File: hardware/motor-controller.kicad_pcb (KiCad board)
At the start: 2 copper layers, 45 parts, among them P102 SWD, P103 EDISON-BULB-E10, P104 FTDI-PLUG, U201 IRLML2803TRPBF, U202 IRLML2803TRPBF, U203 7408, U204 MC33926, U205 MC33926, U206 74AHC541D

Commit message: add footprints for motor connectors
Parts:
- added P201: P06-MOTOR, kicadlib:JST-S6B-PH-K, F.Cu at (144.5, 88.9)
- added P202: P06-MOTOR, kicadlib:JST-S6B-PH-K, F.Cu at (166.8, 85.9)
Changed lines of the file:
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@@
 (kicad_pcb (version 4) (host pcbnew "(after 2015-may-25 BZR unknown)-product")
   (general
-    (links 132)
-    (no_connects 132)
+    (links 144)
+    (no_connects 144)
     (area 0 0 0 0)
     (thickness 1.6)
@@
     (tracks 0)
     (zones 0)
-    (modules 45)
+    (modules 47)
     (nets 69)
   )
@@
       (net 1 +3.3V))
   )
+  (module kicadlib:JST-S6B-PH-K (layer F.Cu)
+    (at 144.5 88.9)
+    (fp_text reference P201 (at -4.8 1.2) (layer F.SilkS)
+      (effects (font (size 0.6 0.6) (thickness 0.1)))
+    )
+    (fp_text value P06-MOTOR (at 0 -2.8) (layer F.Fab)
+      (effects (font (size 0.6 0.6) (thickness 0.1)))
+    )
+    (fp_line (start -7.2 -11.4) (end -7.2 1.8) (layer F.CrtYd) (width 0.15))
+    (fp_line (start -7.2 1.8) (end 7.2 1.8) (layer F.CrtYd) (width 0.15))
+    (fp_line (start 7.2 1.8) (end 7.2 -11.4) (layer F.CrtYd) (width 0.15))
+    (fp_line (start 7.2 -11.4) (end -7.2 -11.4) (layer F.CrtYd) (width 0.15))
+    (fp_line (start 6.95 1.6) (end 6.2 1.6) (layer F.SilkS) (width 0.15))
+    (fp_line (start 6.2 1.6) (end 6.2 0) (layer F.SilkS) (width 0.15))
+    (fp_line (start -6.95 1.6) (end -6.2 1.6) (layer F.SilkS) (width 0.15))
+    (fp_line (start -6.2 1.6) (end -6.2 0) (layer F.SilkS) (width 0.15))
+    (fp_line (start -6.2 0) (end 6.2 0) (layer F.SilkS) (width 0.15))
+    (fp_line (start -6.95 -6) (end 6.95 -6) (layer F.SilkS) (width 0.15))
+    (fp_line (start 6.95 -6) (end 6.95 1.6) (layer F.SilkS) (width 0.15))
+    (fp_line (start -6.95 -6) (end -6.95 1.6) (layer F.SilkS) (width 0.15))
+    (pad 1 thru_hole circle (at 5 0) (size 1.3 1.3) (drill 0.7) (layers *.Cu *.Mask F.SilkS)
+      (net 46 "Net-(P201-Pad1)"))
+    (pad 2 thru_hole circle (at 3 0) (size 1.3 1.3) (drill 0.7) (layers *.Cu *.Mask F.SilkS)
+      (net 49 "Net-(P201-Pad2)"))
+    (pad 3 thru_hole circle (at 1 0) (size 1.3 1.3) (drill 0.7) (layers *.Cu *.Mask F.SilkS)
+      (net 11 +5V))
+    (pad 4 thru_hole circle (at -1 0) (size 1.3 1.3) (drill 0.7) (layers *.Cu *.Mask F.SilkS)
+      (net 2 GNDPWR))
+    (pad 5 thru_hole circle (at -3 0) (size 1.3 1.3) (drill 0.7) (layers *.Cu *.Mask F.SilkS)
+      (net 57 "Net-(P201-Pad5)"))
+    (pad 6 thru_hole circle (at -5 0) (size 1.3 1.3) (drill 0.7) (layers *.Cu *.Mask F.SilkS)
+      (net 58 "Net-(P201-Pad6)"))
+  )
+  (module kicadlib:JST-S6B-PH-K (layer F.Cu)
+    (at 166.8 85.9)
+    (fp_text reference P202 (at -4.8 1.2) (layer F.SilkS)
+      (effects (font (size 0.6 0.6) (thickness 0.1)))
+    )
+    (fp_text value P06-MOTOR (at 0 -2.8) (layer F.Fab)
+      (effects (font (size 0.6 0.6) (thickness 0.1)))
+    )
+    (fp_line (start -7.2 -11.4) (end -7.2 1.8) (layer F.CrtYd) (width 0.15))
+    (fp_line (start -7.2 1.8) (end 7.2 1.8) (layer F.CrtYd) (width 0.15))
+    (fp_line (start 7.2 1.8) (end 7.2 -11.4) (layer F.CrtYd) (width 0.15))
+    (fp_line (start 7.2 -11.4) (end -7.2 -11.4) (layer F.CrtYd) (width 0.15))
+    (fp_line (start 6.95 1.6) (end 6.2 1.6) (layer F.SilkS) (width 0.15))
+    (fp_line (start 6.2 1.6) (end 6.2 0) (layer F.SilkS) (width 0.15))
+    (fp_line (start -6.95 1.6) (end -6.2 1.6) (layer F.SilkS) (width 0.15))
+    (fp_line (start -6.2 1.6) (end -6.2 0) (layer F.SilkS) (width 0.15))
+    (fp_line (start -6.2 0) (end 6.2 0) (layer F.SilkS) (width 0.15))
+    (fp_line (start -6.95 -6) (end 6.95 -6) (layer F.SilkS) (width 0.15))
+    (fp_line (start 6.95 -6) (end 6.95 1.6) (layer F.SilkS) (width 0.15))
+    (fp_line (start -6.95 -6) (end -6.95 1.6) (layer F.SilkS) (width 0.15))
+    (pad 1 thru_hole circle (at 5 0) (size 1.3 1.3) (drill 0.7) (layers *.Cu *.Mask F.SilkS)
+      (net 53 "Net-(P202-Pad1)"))
+    (pad 2 thru_hole circle (at 3 0) (size 1.3 1.3) (drill 0.7) (layers *.Cu *.Mask F.SilkS)
+      (net 56 "Net-(P202-Pad2)"))
+    (pad 3 thru_hole circle (at 1 0) (size 1.3 1.3) (drill 0.7) (layers *.Cu *.Mask F.SilkS)
+      (net 11 +5V))
+    (pad 4 thru_hole circle (at -1 0) (size 1.3 1.3) (drill 0.7) (layers *.Cu *.Mask F.SilkS)
+      (net 2 GNDPWR))
+    (pad 5 thru_hole circle (at -3 0) (size 1.3 1.3) (drill 0.7) (layers *.Cu *.Mask F.SilkS)
+      (net 59 "Net-(P202-Pad5)"))
+    (pad 6 thru_hole circle (at -5 0) (size 1.3 1.3) (drill 0.7) (layers *.Cu *.Mask F.SilkS)
+      (net 60 "Net-(P202-Pad6)"))
+  )
 )

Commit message: add package for battery and compass
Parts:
- added P101: BATTERY, kicadlib:TECONN-2-1445098-2, F.Cu at (116.5, 91.8)
- added U101: STM32F030K6T6, kicadlib:QFP80P900X900X160-32N, F.Cu at (151.0, 117.2)
- added U102: ST-LIS3MDL, kicadlib:LGA12S50P4X4_192X192X100, F.Cu at (187.7, 85.8)
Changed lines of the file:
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@@
 (kicad_pcb (version 4) (host pcbnew "(after 2015-may-25 BZR unknown)-product")
   (general
-    (links 144)
-    (no_connects 144)
+    (links 185)
+    (no_connects 185)
     (area 0 0 0 0)
     (thickness 1.6)
@@
     (tracks 0)
     (zones 0)
-    (modules 47)
-    (nets 69)
+    (modules 50)
+    (nets 74)
   )
   (page A4)
@@
   (net 67 /drivers/MOTORLCHB)
   (net 68 /drivers/MOTORLCHA)
+  (net 69 "Net-(U101-Pad2)")
+  (net 70 "Net-(U101-Pad3)")
+  (net 71 "Net-(U101-Pad6)")
+  (net 72 /COMPASSDRDY)
+  (net 73 /COMPASSINT)
   (net_class Default "This is the default net class."
     (clearance 0.2)
@@
     (add_net +3.3V)
     (add_net +5V)
+    (add_net /COMPASSDRDY)
+    (add_net /COMPASSINT)
     (add_net /I2CSCL)
     (add_net /I2CSDA)
@@
     (add_net "Net-(R213-Pad1)")
     (add_net "Net-(R214-Pad1)")
+    (add_net "Net-(U101-Pad2)")
+    (add_net "Net-(U101-Pad3)")
+    (add_net "Net-(U101-Pad6)")
     (add_net "Net-(U203-Pad11)")
     (add_net "Net-(U203-Pad3)")
@@
       (net 60 "Net-(P202-Pad6)"))
   )
+  (module kicadlib:TECONN-2-1445098-2 (layer F.Cu)
+    (at 116.5 91.8)
+    (fp_text reference P101 (at 7.112 -1.27 90) (layer F.SilkS)
+      (effects (font (size 0.6 0.6) (thickness 0.1)))
+    )
+    (fp_text value BATTERY (at 1.397 -1.905) (layer F.Fab)
+      (effects (font (size 0.6 0.6) (thickness 0.1)))
+    )
+    (fp_line (start -3.57 -7.75) (end -3.57 0) (layer F.SilkS) (width 0.1))
+    (fp_line (start 6.57 0) (end 6.57 -7.75) (layer F.SilkS) (width 0.1))
+    (fp_line (start -4.07 -9.42) (end 7.07 -9.42) (layer F.CrtYd) (width 0.1))
+    (fp_line (start 7.07 -9.42) (end 7.07 1.325) (layer F.CrtYd) (width 0.1))
+    (fp_line (start 7.07 1.325) (end -4.07 1.325) (layer F.CrtYd) (width 0.1))
+    (fp_line (start -4.07 1.325) (end -4.07 -9.42) (layer F.CrtYd) (width 0.1))
+    (fp_line (start -3.57 -8.92) (end 6.57 -8.92) (layer Dwgs.User) (width 0.1))
+    (fp_line (start 6.57 -8.92) (end 6.57 -7.75) (layer Dwgs.User) (width 0.1))
+    (fp_line (start 6.57 0) (end -3.57 0) (layer F.SilkS) (width 0.1))
+    (fp_line (start -3.57 -7.75) (end -3.57 -8.92) (layer Dwgs.User) (width 0.1))
+    (pad 1 thru_hole circle (at 0 0) (size 1.65 1.65) (drill 1) (layers *.Cu *.Mask F.SilkS)
+      (net 4 Vcc))
+    (pad 2 thru_hole circle (at 3 0) (size 1.65 1.65) (drill 1) (layers *.Cu *.Mask F.SilkS)
+      (net 2 GNDPWR))
+    (pad "" thru_hole circle (at 1.5 -4.32) (size 3.05 3.05) (drill 3.05) (layers *.Cu *.Mask F.SilkS))
+  )
+  (module kicadlib:QFP80P900X900X160-32N (layer F.Cu)
+    (at 151 117.2)
+    (clearance 0.24)
+    (fp_text reference U101 (at 0 5.715) (layer F.SilkS)
+      (effects (font (size 0.6 0.6) (thickness 0.1)))
+    )
+    (fp_text value STM32F030K6T6 (at 0 0) (layer F.SilkS)
+      (effects (font (size 0.6 0.6) (thickness 0.1)))
+    )
+    (fp_circle (center -4.8 -3.6) (end -4.7 -3.6) (layer F.SilkS) (width 0.3))
+    (fp_circle (center -2.2 -2.2) (end -2 -2.2) (layer F.SilkS) (width 0.5))
+    (fp_line (start -5.2 -5.2) (end 5.2 -5.2) (layer Cmts.User) (width 0.1))
+    (fp_line (start 5.2 -5.2) (end 5.2 5.2) (layer Cmts.User) (width 0.1))
+    (fp_line (start 5.2 5.2) (end -5.2 5.2) (layer Cmts.User) (width 0.1))
+    (fp_line (start -5.2 5.2) (end -5.2 -5.2) (layer Cmts.User) (width 0.1))
+    (fp_line (start -3.1 -3.1) (end 3.1 -3.1) (layer F.SilkS) (width 0.1))
+    (fp_line (start 3.1 -3.1) (end 3.1 3.1) (layer F.SilkS) (width 0.1))
+    (fp_line (start 3.1 3.1) (end -3.1 3.1) (layer F.SilkS) (width 0.1))
+    (fp_line (start -3.1 3.1) (end -3.1 -3.1) (layer F.SilkS) (width 0.1))
+    (pad 1 smd rect (at -4.2 -2.8) (size 1.5 0.55) (layers F.Cu F.Paste F.Mask)
+      (net 1 +3.3V))
+    (pad 2 smd rect (at -4.2 -2) (size 1.5 0.55) (layers F.Cu F.Paste F.Mask)
+      (net 69 "Net-(U101-Pad2)"))
+    (pad 3 smd rect (at -4.2 -1.2) (size 1.5 0.55) (layers F.Cu F.Paste F.Mask)
+      (net 70 "Net-(U101-Pad3)"))
+    (pad 4 smd rect (at -4.2 -0.4) (size 1.5 0.55) (layers F.Cu F.Paste F.Mask)
+      (net 9 /NRST))
+    (pad 5 smd rect (at -4.2 0.4) (size 1.5 0.55) (layers F.Cu F.Paste F.Mask)
+      (net 1 +3.3V))
+    (pad 6 smd rect (at -4.2 1.2) (size 1.5 0.55) (layers F.Cu F.Paste F.Mask)
+      (net 71 "Net-(U101-Pad6)"))
+    (pad 7 smd rect (at -4.2 2) (size 1.5 0.55) (layers F.Cu F.Paste F.Mask)
+      (net 12 /NIRQ))
+    (pad 8 smd rect (at -4.2 2.8) (size 1.5 0.55) (layers F.Cu F.Paste F.Mask)
+      (net 20 /USARTTX))
+    (pad 9 smd rect (at -2.8 4.2) (size 0.55 1.5) (layers F.Cu F.Paste F.Mask)
+      (net 19 /USARTRX))
+    (pad 10 smd rect (at -2 4.2) (size 0.55 1.5) (layers F.Cu F.Paste F.Mask)
+      (net 13 /SPICS))
+    (pad 11 smd rect (at -1.2 4.2) (size 0.55 1.5) (layers F.Cu F.Paste F.Mask)
+      (net 16 /SPISCK))
+    (pad 12 smd rect (at -0.4 4.2) (size 0.55 1.5) (layers F.Cu F.Paste F.Mask)
+      (net 14 /SPIMISO))
+    (pad 13 smd rect (at 0.4 4.2) (size 0.55 1.5) (layers F.Cu F.Paste F.Mask)
+      (net 15 /SPIMOSI))
+    (pad 14 smd rect (at 1.2 4.2) (size 0.55 1.5) (layers F.Cu F.Paste F.Mask)
+      (net 68 /drivers/MOTORLCHA))
+    (pad 15 smd rect (at 2 4.2) (size 0.55 1.5) (layers F.Cu F.Paste F.Mask)
+      (net 67 /drivers/MOTORLCHB))
+    (pad 16 smd rect (at 2.8 4.2) (size 0.55 1.5) (layers F.Cu F.Paste F.Mask)
+      (net 2 GNDPWR))
+    (pad 17 smd rect (at 4.2 2.8) (size 1.5 0.55) (layers F.Cu F.Paste F.Mask)
+      (net 1 +3.3V))
+    (pad 18 smd rect (at 4.2 2) (size 1.5 0.55) (layers F.Cu F.Paste F.Mask)
+      (net 28 /drivers/MOTORLPWM))
+    (pad 19 smd rect (at 4.2 1.2) (size 1.5 0.55) (layers F.Cu F.Paste F.Mask)
+      (net 24 /drivers/MOTORLDIR))
+    (pad 20 smd rect (at 4.2 0.4) (size 1.5 0.55) (layers F.Cu F.Paste F.Mask)
+      (net 29 /drivers/MOTORRPWM))
+    (pad 21 smd rect (at 4.2 -0.4) (size 1.5 0.55) (layers F.Cu F.Paste F.Mask)
+      (net 25 /drivers/MOTORRDIR))
+    (pad 22 smd rect (at 4.2 -1.2) (size 1.5 0.55) (layers F.Cu F.Paste F.Mask)
+      (net 45 /drivers/MOTOREN))
+    (pad 23 smd rect (at 4.2 -2) (size 1.5 0.55) (layers F.Cu F.Paste F.Mask)
+      (net 8 /SWDIO))
+    (pad 24 smd rect (at 4.2 -2.8) (size 1.5 0.55) (layers F.Cu F.Paste F.Mask)
+      (net 7 /SWCLK))
+    (pad 25 smd rect (at 2.8 -4.2) (size 0.55 1.5) (layers F.Cu F.Paste F.Mask)
+      (net 72 /COMPASSDRDY))
+    (pad 26 smd rect (at 2 -4.2) (size 0.55 1.5) (layers F.Cu F.Paste F.Mask)
+      (net 73 /COMPASSINT))
+    (pad 27 smd rect (at 1.2 -4.2) (size 0.55 1.5) (layers F.Cu F.Paste F.Mask)
+      (net 66 /drivers/MOTORRCHA))
+    (pad 28 smd rect (at 0.4 -4.2) (size 0.55 1.5) (layers F.Cu F.Paste F.Mask)
+      (net 65 /drivers/MOTORRCHB))
+    (pad 29 smd rect (at -0.4 -4.2) (size 0.55 1.5) (layers F.Cu F.Paste F.Mask)
+      (net 23 /I2CSCL))
+    (pad 30 smd rect (at -1.2 -4.2) (size 0.55 1.5) (layers F.Cu F.Paste F.Mask)
+      (net 22 /I2CSDA))
+    (pad 31 smd rect (at -2 -4.2) (size 0.55 1.5) (layers F.Cu F.Paste F.Mask)
+      (net 2 GNDPWR))
+    (pad 32 smd rect (at -2.8 -4.2) (size 0.55 1.5) (layers F.Cu F.Paste F.Mask)
+      (net 2 GNDPWR))
+  )
+  (module kicadlib:LGA12S50P4X4_192X192X100 (layer F.Cu)
+    (at 187.7 85.8)
+    (fp_text reference U102 (at 0.2 -1.8) (layer F.SilkS)
+      (effects (font (size 0.6 0.6) (thickness 0.1)))
+    )
+    (fp_text value ST-LIS3MDL (at 0 0) (layer F.Fab)
+      (effects (font (size 0.6 0.6) (thickness 0.1)))
+    )
+    (fp_circle (center -1.6 -1.6) (end -1.4 -1.6) (layer F.SilkS) (width 0.4))
+    (fp_line (start -2 -2) (end 2 -2) (layer F.CrtYd) (width 0.15))
+    (fp_line (start 2 -2) (end 2 2) (layer F.CrtYd) (width 0.15))
+    (fp_line (start 2 2) (end -2 2) (layer F.CrtYd) (width 0.15))
+    (fp_line (start -2 2) (end -2 -2) (layer F.CrtYd) (width 0.15))
+    (fp_line (start -1 -1) (end 1 -1) (layer F.SilkS) (width 0.15))
+    (fp_line (start 1 -1) (end 1 1) (layer F.SilkS) (width 0.15))
+    (fp_line (start 1 1) (end -1 1) (layer F.SilkS) (width 0.15))
+    (fp_line (start -1 1) (end -1 -1) (layer F.SilkS) (width 0.15))
+    (pad 1 smd rect (at -0.75 -0.75) (size 0.25 0.25) (layers F.Cu F.Paste F.Mask)
+      (net 23 /I2CSCL))
+    (pad 2 smd rect (at -0.75 -0.25) (size 0.25 0.25) (layers F.Cu F.Paste F.Mask)
+      (net 2 GNDPWR))
+    (pad 3 smd rect (at -0.75 0.25) (size 0.25 0.25) (layers F.Cu F.Paste F.Mask)
+      (net 2 GNDPWR))
+    (pad 4 smd rect (at -0.75 0.75) (size 0.25 0.25) (layers F.Cu F.Paste F.Mask)
+      (net 3 "Net-(C106-Pad1)"))
+    (pad 5 smd rect (at -0.25 0.75) (size 0.25 0.25) (layers F.Cu F.Paste F.Mask)
+      (net 1 +3.3V))
+    (pad 6 smd rect (at 0.25 0.75) (size 0.25 0.25) (layers F.Cu F.Paste F.Mask)
+      (net 1 +3.3V))
+    (pad 7 smd rect (at 0.75 0.75) (size 0.25 0.25) (layers F.Cu F.Paste F.Mask)
+      (net 73 /COMPASSINT))
+    (pad 8 smd rect (at 0.75 0.25) (size 0.25 0.25) (layers F.Cu F.Paste F.Mask)
+      (net 72 /COMPASSDRDY))
+    (pad 9 smd rect (at 0.75 -0.25) (size 0.25 0.25) (layers F.Cu F.Paste F.Mask)
+      (net 1 +3.3V))
+    (pad 10 smd rect (at 0.75 -0.75) (size 0.25 0.25) (layers F.Cu F.Paste F.Mask)
+      (net 1 +3.3V))
+    (pad 11 smd rect (at 0.25 -0.75) (size 0.25 0.25) (layers F.Cu F.Paste F.Mask)
+      (net 22 /I2CSDA))
+    (pad 12 smd rect (at -0.25 -0.75) (size 0.25 0.25) (layers F.Cu F.Paste F.Mask)
+      (net 2 GNDPWR))
+  )
 )

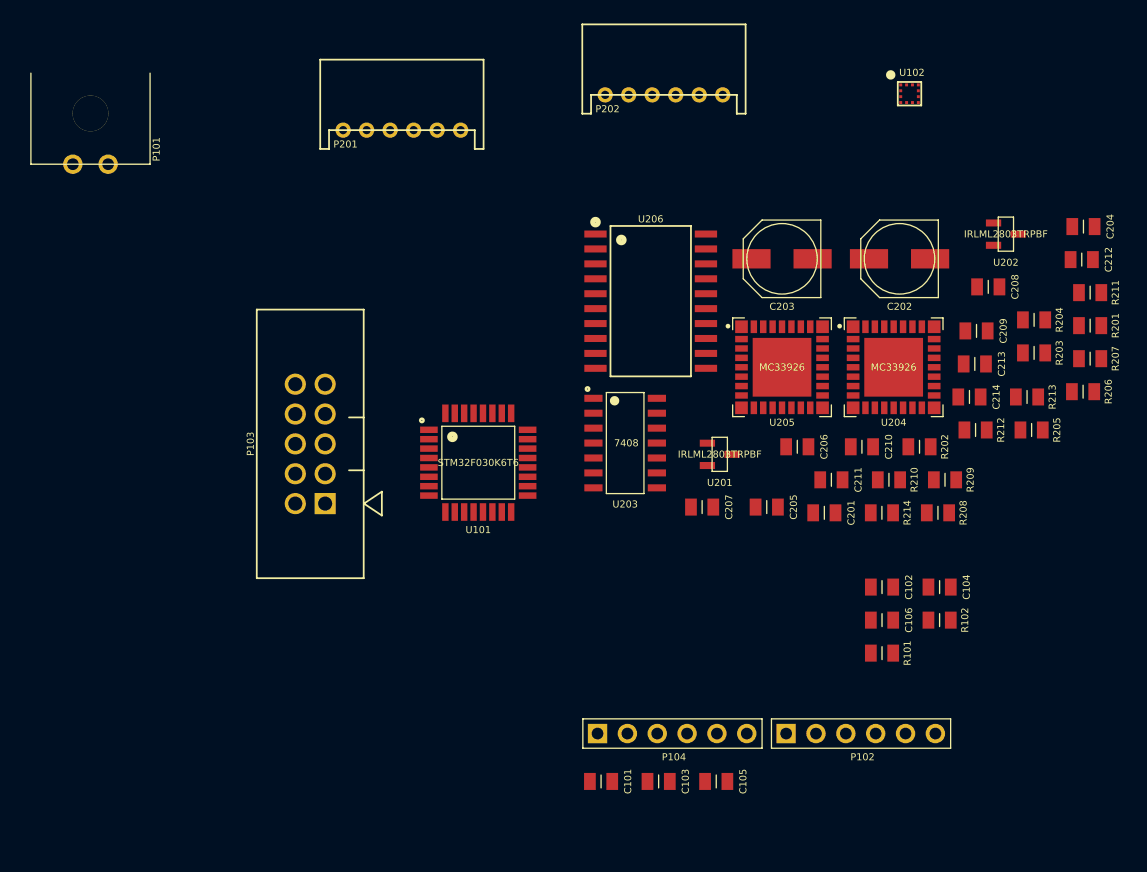
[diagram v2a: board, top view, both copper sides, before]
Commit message: initial component placement
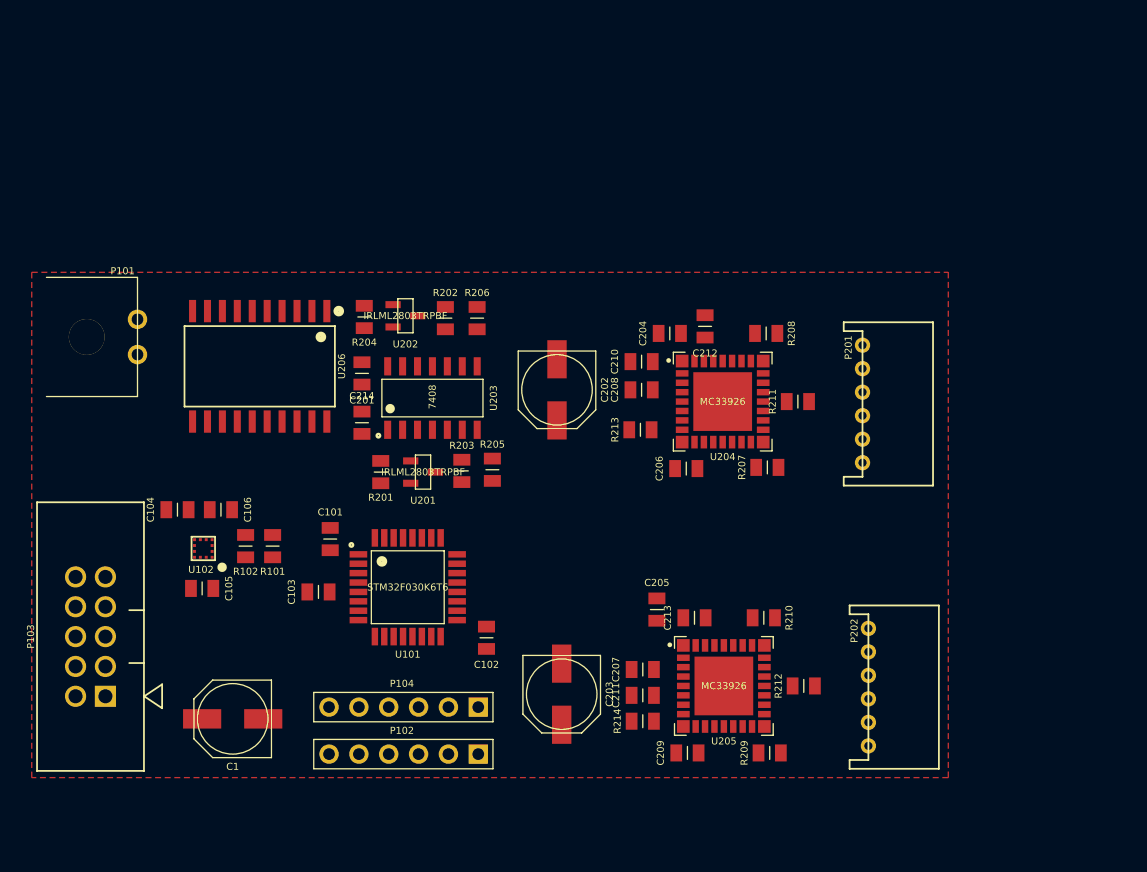
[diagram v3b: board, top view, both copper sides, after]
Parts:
- added C1: 100uF, kicadlib:CAPAE660X790N, F.Cu at (130.1, 139.0)
- moved U102 71.5 mm to (127.6, 124.5), turned to 180 degrees
- moved C104 65.2 mm to (125.4, 121.2), turned to 180 degrees
- moved R201 61.6 mm to (142.7, 118.0), turned to 270 degrees
- moved R102 59.4 mm to (131.2, 124.3), turned to 270 degrees
- moved C106 57.0 mm to (129.1, 121.2)
- moved R204 57.0 mm to (141.3, 104.8), turned to 270 degrees
- moved P202 53.3 mm to (184.2, 136.3), turned to 270 degrees
- moved R101 52.7 mm to (133.5, 124.3), turned to 270 degrees
- moved R206 51.9 mm to (150.9, 104.9), turned to 90 degrees
- moved C214 51.7 mm to (141.1, 113.8), turned to 90 degrees
- moved U202 51.6 mm to (144.8, 104.7)
- moved R203 49.7 mm to (149.6, 117.9), turned to 90 degrees
- moved C105 46.7 mm to (127.5, 127.9)
- moved R205 46.0 mm to (152.2, 117.8), turned to 90 degrees
- moved P201 45.6 mm to (183.7, 112.2), turned to 270 degrees
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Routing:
- added copper zone on F.Cu, net GNDPWR

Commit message: initial layout
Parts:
- moved P202 28.4 mm to (178.2, 108.5)
- moved C205 25.0 mm to (164.2, 104.8), turned to 180 degrees
- moved C207 24.3 mm to (161.2, 110.8)
- moved C211 24.3 mm to (161.2, 113.0)
- moved C209 24.2 mm to (164.8, 118.0)
- moved R209 24.2 mm to (171.8, 118.0)
- moved R212 24.1 mm to (174.2, 112.5)
- moved U205 24.1 mm to (167.8, 112.5)
- moved C213 24.0 mm to (164.2, 107.0)
- moved C203 23.9 mm to (155.5, 113.2)
- moved R214 23.7 mm to (161.2, 115.8)
- moved R210 23.7 mm to (171.8, 107.0)
- moved C210 22.0 mm to (161.2, 130.2)
- moved C208 21.8 mm to (161.2, 132.5)
- moved C212 21.8 mm to (164.2, 126.5), turned to 180 degrees
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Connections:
- net Net-(P201-Pad1) renamed /drivers/MOTORL-
- net Net-(P201-Pad2) renamed /drivers/MOTORL+
- net Net-(P202-Pad1) renamed /drivers/MOTORR-
- net Net-(P202-Pad2) renamed /drivers/MOTORR+
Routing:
- net +3.3V: track 0.00 -> 216.6 mm, vias 0 -> 5
- net Vcc: track 0.00 -> 187.9 mm
- net GNDPWR: track 0.00 -> 149.5 mm, vias 0 -> 48
- net +5V: track 0.00 -> 101.6 mm
- net /NRST: track 0.00 -> 56.9 mm, vias 0 -> 1
- net /drivers/MOTOREN: track 0.00 -> 52.8 mm, vias 0 -> 5
- net Net-(P202-Pad5): track 0.00 -> 51.9 mm, vias 0 -> 1
- net Net-(P202-Pad6): track 0.00 -> 51.7 mm, vias 0 -> 1
- net Net-(P201-Pad5): track 0.00 -> 47.3 mm, vias 0 -> 1
- net Net-(P201-Pad6): track 0.00 -> 46.7 mm, vias 0 -> 1
- net /drivers/MOTORLCHB: track 0.00 -> 43.2 mm, vias 0 -> 4
- net /drivers/MOTORLCHA: track 0.00 -> 42.2 mm, vias 0 -> 2
- net /drivers/MOTORRPWM: track 0.00 -> 41.7 mm, vias 0 -> 2
- net /drivers/MOTORRDIR: track 0.00 -> 35.0 mm
- net /SPISCK: track 0.00 -> 34.9 mm
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- added copper zone on B.Cu, net GNDPWR
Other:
- board outline added: 71.2 x 43 mm
- net class Default: clearance 0.2 -> 0.2032; trace_width 0.25 -> 0.2032; via_dia 0.6 -> 0.6858; via_drill 0.4 -> 0.3302
- net class VCC added: clearance 0.254, trace_width 0.508, via_dia 0.6858, via_drill 0.3302
- rule trace_clearance: 0.2 -> 0.2032

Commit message: more layout
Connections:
- P201 pad 5: Net-(P201-Pad5) -> /drivers/MOTORLCHA
- P201 pad 6: Net-(P201-Pad6) -> /drivers/MOTORLCHB
- P202 pad 5: Net-(P202-Pad5) -> /drivers/MOTORRCHA
- P202 pad 6: Net-(P202-Pad6) -> /drivers/MOTORRCHB
- U206 pad 2: Net-(P201-Pad5) -> /drivers/MOTORLCHA
- U206 pad 3: Net-(P201-Pad6) -> /drivers/MOTORLCHB
- U206 pad 4: Net-(P202-Pad5) -> /drivers/MOTORRCHA
- U206 pad 5: Net-(P202-Pad6) -> /drivers/MOTORRCHB
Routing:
- net Net-(P202-Pad5): track 51.9 -> 0.00 mm, vias 1 -> 0
- net /drivers/MOTORRCHA: track 29.9 -> 81.9 mm, vias 4 -> 5
- net Net-(P202-Pad6): track 51.7 -> 0.00 mm, vias 1 -> 0
- net /drivers/MOTORRCHB: track 28.4 -> 80.1 mm, vias 2 -> 3
- net Net-(P201-Pad5): track 47.3 -> 0.00 mm, vias 1 -> 0
- net /drivers/MOTORLCHA: track 42.2 -> 89.6 mm, vias 2 -> 3
- net /drivers/MOTORLCHB: track 43.2 -> 89.8 mm, vias 4 -> 5
- net Net-(P201-Pad6): track 46.7 -> 0.00 mm, vias 1 -> 0
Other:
- board text added: "+"
- board text added: "+3.3V"
- board text added: "+5V"
- board text added: "5V-28V"
- board text added: "CHA"
- board text added: "CHB"
- board text added: "GND"
- board text added: "M+"
- board text added: "M-"
- board text added: "RX"
- board text added: "SWD"
- board text added: "TX"
- board text added: "USART"
